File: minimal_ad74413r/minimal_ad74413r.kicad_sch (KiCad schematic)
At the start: 17 parts, among them U8 AD74413RBCPZ

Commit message: backup
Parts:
- added TP1, TP10, TP11, TP12, TP13, TP14, TP15, TP16, TP17, TP18, TP19, TP2, TP20, TP21, TP22, TP23, TP24, TP3, TP4, TP5, TP6, TP7, TP8, TP9: TestPoint, test_point_footprints:TestPoint_THTPad_Castelated, symbol UNITED_TEST_POINTS:TestPoint_Castelated
- C82: footprint footprints:C_0603_1608Metric -> capacitor_footprints:C_0603_1608Metric; symbol CAPACITORS_DATA_BASE:C_000011 -> UNITED_CAPACITORS_DATA_BASE:C_GRM188R71A334KA61D; Case Code - in (none) -> 0603; Case Code - mm (none) -> 1608; Dielectric (none) -> X7R; Manufacturer Murata -> Murata Electronics; Series (none) -> GRM188R71A; Symbol Name C_000011 -> C_GRM188R71A334KA61D; Trustedparts Search (none) -> https://www.trustedparts.com/en/search/GRM188R71A334KA61D; Voltage Rating (none) -> 10V
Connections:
- net GNDA: now also TP10.1, TP15.1, TP16.1, TP17.1, TP18.1, TP24.1
- net GPO_A: now also TP19.1
- net GPO_B: now also TP20.1
- net GPO_C: now also TP21.1
- net GPO_D: now also TP22.1
- net SCLK: now also TP4.1
- net SDI: now also TP3.1
- net SDO: now also TP8.1
- net ~{ADC_RDY}: now also TP7.1
- net ~{ALERT}: now also TP6.1
- net ~{LDAC}: now also TP5.1
- net ~{RESET}: now also TP1.1
- net ~{SYNC}: now also TP2.1
- net 3V3_ISO renamed 3V3
- net 3V3: now also TP23.1, TP9.1
- new net CHANNEL_1: TP11.1
- new net CHANNEL_2: TP12.1
- new net CHANNEL_3: TP13.1
- new net CHANNEL_4: TP14.1
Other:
- added sheet Front End Channel 1 (Front End Channel 1.kicad_sch)
- added sheet Front End Channel 2 (Front End Channel 1.kicad_sch)
- added sheet Front End Channel 3 (Front End Channel 1.kicad_sch)
- added sheet Front End Channel 4 (Front End Channel 1.kicad_sch)
- moved on the sheet: C81, C83, C84, C85, C86, C87, C88, C89, C90, C91, C92, C93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

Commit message: backup
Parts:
- added TP25, TP26: TestPoint, test_point_footprints:TestPoint_THTPad_Castelated, symbol UNITED_TEST_POINTS:TestPoint_Castelated
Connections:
- net 3V3: no longer TP23.1
- net GNDA: now also TP25.1, TP26.1; no longer TP24.1
- net VDD_24V: now also TP23.1, TP24.1

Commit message: Backup
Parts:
- added J1, J2, J3, J4: CLP-102-02-G-D-BE, connector_footprints:CLP-102-02-G-D-BE, symbol UNITED_CONNECTORS_DATA_BASE:J_CLP-102-02-G-D-BE
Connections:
- net CHANNEL_1: now also J1.1, J1.3
- net CHANNEL_2: now also J2.2, J2.4
- net CHANNEL_3: now also J3.1, J3.3
- net CHANNEL_4: now also J4.2, J4.4
- net GNDA: now also J1.2, J1.4, J2.1, J2.3, J3.2, J3.4, J4.1, J4.3
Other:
- moved on the sheet: TP11, TP12, TP13, TP14, TP15, TP16, TP17, TP18

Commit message: Backup
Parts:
- added J5, J6: CLP-102-02-G-D-BE, connector_footprints:CLP-102-02-G-D-BE, symbol UNITED_CONNECTORS_DATA_BASE:J_CLP-102-02-G-D-BE
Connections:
- net GNDA: now also J5.1, J5.3, J6.2, J6.4
- net VDD_24V: now also J5.2, J5.4, J6.1, J6.3
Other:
- moved on the sheet: TP23, TP24, TP25, TP26

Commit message: Minor updates
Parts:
- added J7: CLP-114-02-G-D-BE, connector_footprints:CLP-114-02-G-D-BE, symbol UNITED_CONNECTORS_DATA_BASE:J_CLP-114-02-G-D-BE
- renumbered C96 to C1, C86 to C14, C85 to C15, C87 to C16, C92 to C17, C95 to C18, C93 to C19, C89 to C2, C94 to C20, C88 to C29, C90 to C3, C84 to C30, C91 to C31, C83 to C32, C82 to C4, C81 to C5, J2 to J1, J3 to J2, J6 to J3, J5 to J4, J4 to J5, J1 to J6, TP13 to TP1, TP18 to TP10, TP15 to TP11, TP11 to TP12, TP8 to TP13, TP7 to TP14, TP6 to TP15, TP10 to TP16, TP9 to TP17, TP5 to TP18, TP4 to TP19, TP17 to TP2, TP3 to TP20, TP2 to TP21, TP1 to TP22, TP22 to TP23, TP21 to TP24, TP20 to TP25, TP19 to TP26, TP16 to TP3, TP12 to TP4, TP25 to TP5, TP26 to TP6, TP24 to TP7, TP23 to TP8, TP14 to TP9, U8 to U1
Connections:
- net 3V3: now also J7.10, J7.9
- net GNDA: now also J7.7, J7.8
- net GPO_A: now also J7.27, J7.28
- net GPO_B: now also J7.25, J7.26
- net GPO_C: now also J7.23, J7.24
- net GPO_D: now also J7.21, J7.22
- net SCLK: now also J7.13, J7.14
- net SDI: now also J7.15, J7.16
- net SDO: now also J7.1, J7.2
- net ~{ADC_RDY}: now also J7.3, J7.4
- net ~{ALERT}: now also J7.5, J7.6
- net ~{LDAC}: now also J7.11, J7.12
- net ~{RESET}: now also J7.19, J7.20
- net ~{SYNC}: now also J7.17, J7.18

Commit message: Minor updates
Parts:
- removed J3, J4: CLP-102-02-G-D-BE, connector_footprints:CLP-102-02-G-D-BE, symbol UNITED_CONNECTORS_DATA_BASE:J_CLP-102-02-G-D-BE
- added J3, J8: CLP-104-02-G-D-BE, connector_footprints:CLP-104-02-G-D-BE, symbol UNITED_CONNECTORS_DATA_BASE:J_CLP-104-02-G-D-BE
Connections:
- net CHANNEL_1: now also J6.4; no longer J6.1
- net CHANNEL_2: now also J1.1; no longer J1.4
- net CHANNEL_3: now also J2.4; no longer J2.1
- net CHANNEL_4: now also J5.1; no longer J5.4
- net GNDA: now also J1.4, J2.1, J5.4, J6.1, J3.1, J3.2, J8.7, J8.8; no longer J1.1, J2.4, J5.1, J6.4
- net VDD_24V: now also J3.3, J3.4, J8.5, J8.6
- no-connect marks 1 -> 9
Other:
- moved on the sheet: C1, C14, C15, C16, C17, C18, C19, C2, C20, C29, C3, C30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

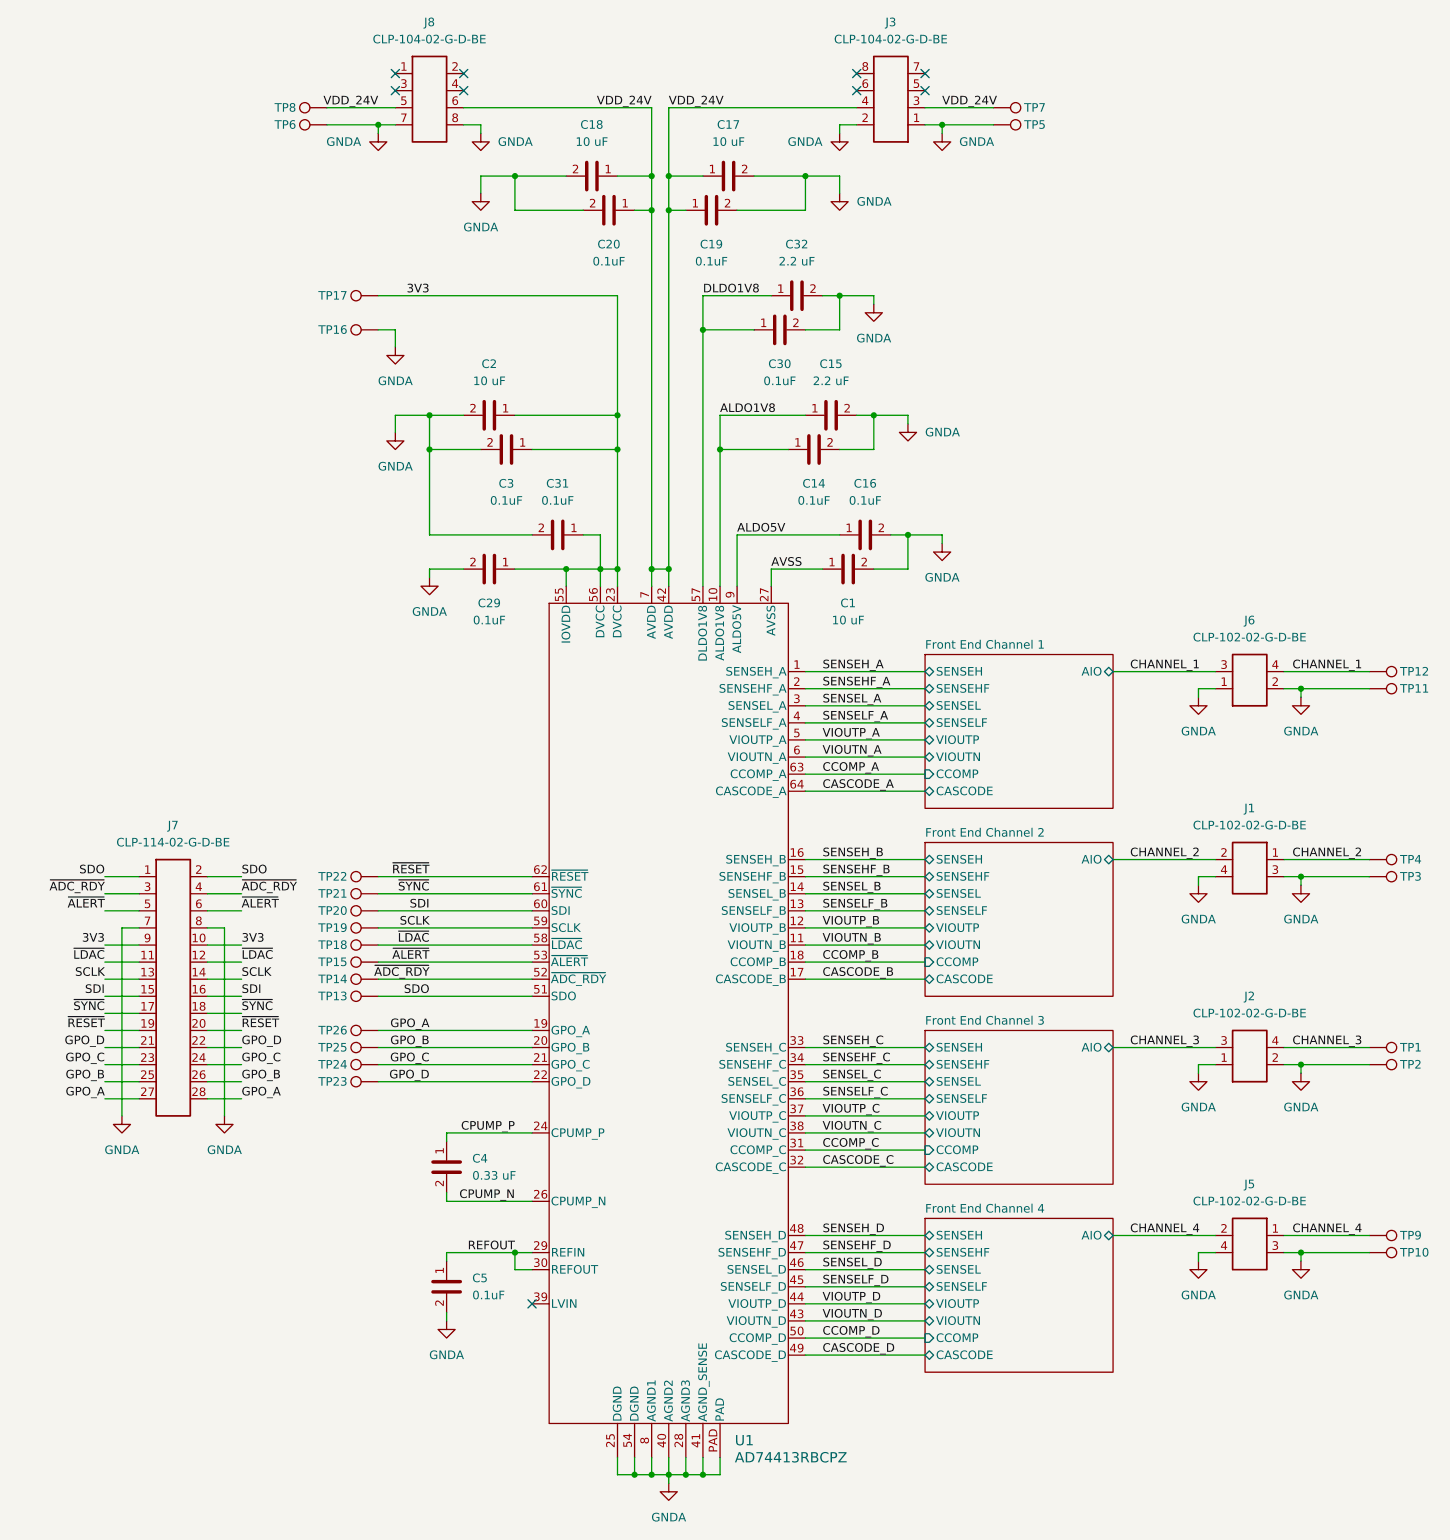
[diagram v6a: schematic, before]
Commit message: Update references in schematic and update subproject commit
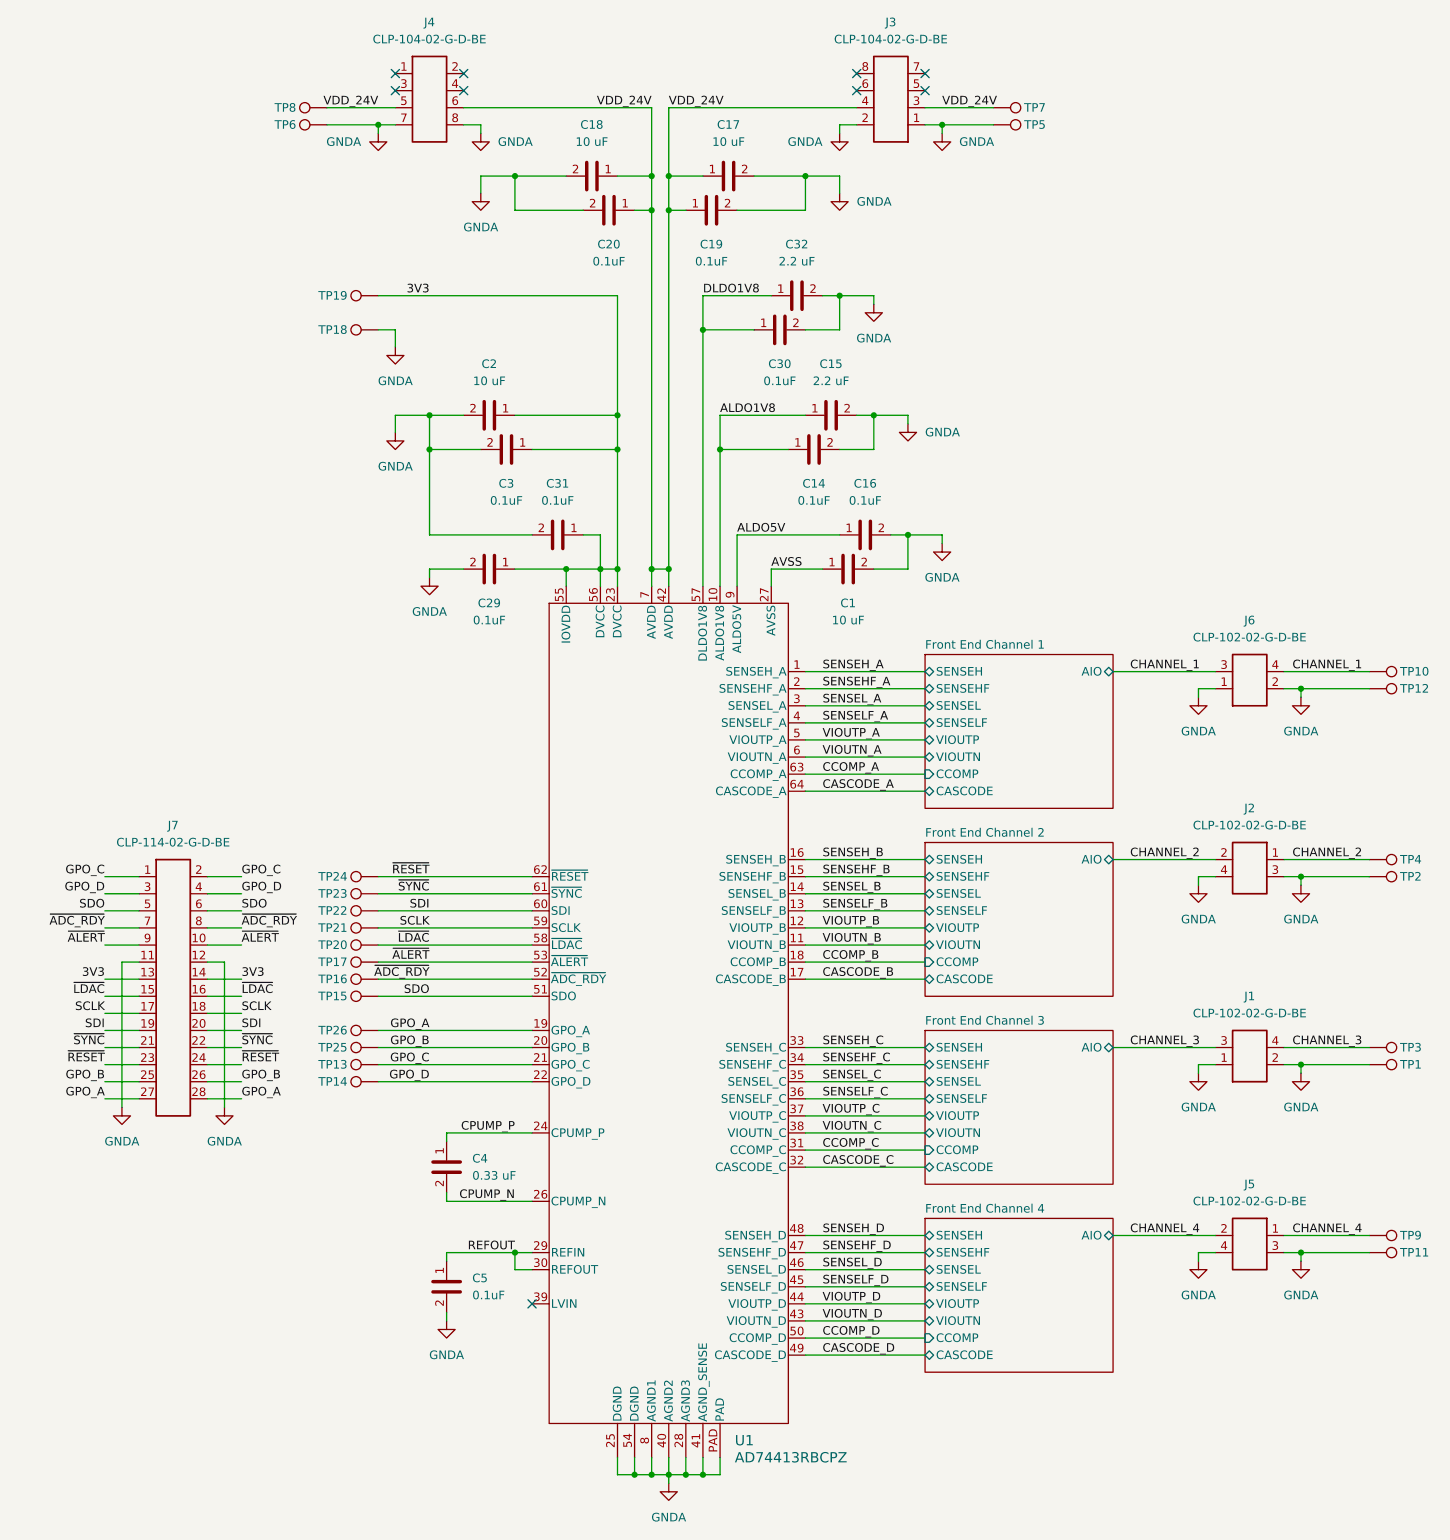
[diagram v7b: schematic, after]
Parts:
- renumbered J2 to J1, J1 to J2, J8 to J4, TP2 to TP1, TP12 to TP10, TP10 to TP11, TP11 to TP12, TP24 to TP13, TP23 to TP14, TP13 to TP15, TP14 to TP16, TP15 to TP17, TP16 to TP18, TP17 to TP19, TP3 to TP2, TP18 to TP20, TP19 to TP21, TP20 to TP22, TP21 to TP23, TP22 to TP24, TP1 to TP3
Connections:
- net 3V3: now also J7.13, J7.14; no longer J7.10, J7.9
- net GNDA: now also J7.11, J7.12; no longer J7.7, J7.8
- net GPO_C: now also J7.1, J7.2; no longer J7.23, J7.24
- net GPO_D: now also J7.3, J7.4; no longer J7.21, J7.22
- net SCLK: now also J7.17, J7.18; no longer J7.13, J7.14
- net SDI: now also J7.19, J7.20; no longer J7.15, J7.16
- net SDO: now also J7.5, J7.6; no longer J7.1, J7.2
- net ~{ADC_RDY}: now also J7.7, J7.8; no longer J7.3, J7.4
- net ~{ALERT}: now also J7.10, J7.9; no longer J7.5, J7.6
- net ~{LDAC}: now also J7.15, J7.16; no longer J7.11, J7.12
- net ~{RESET}: now also J7.23, J7.24; no longer J7.19, J7.20
- net ~{SYNC}: now also J7.21, J7.22; no longer J7.17, J7.18

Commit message: Minor updates to project files
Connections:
- net 3V3: no longer J7.14
- net GNDA: now also J7.10, J7.14, J7.16, J7.18, J7.2, J7.20, J7.22, J7.24, J7.26, J7.28, J7.4, J7.6, J7.8
- net GPO_A: no longer J7.28
- net GPO_B: no longer J7.26
- net GPO_C: no longer J7.2
- net GPO_D: no longer J7.4
- net SCLK: no longer J7.18
- net SDI: no longer J7.20
- net SDO: no longer J7.6
- net ~{ADC_RDY}: no longer J7.8
- net ~{ALERT}: no longer J7.10
- net ~{LDAC}: no longer J7.16
- net ~{RESET}: no longer J7.24
- net ~{SYNC}: no longer J7.22
